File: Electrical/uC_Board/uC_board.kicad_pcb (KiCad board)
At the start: 2 copper layers, 45 x 18 mm, 27 parts, among them J1 card_edge_6p, J2 ArdStripNano, Q1 BC850, SW1 SW_Push, U1 ATmega328PB-AU, U2 AD8620, U3 LM1117MPX-5.0, X1 CSTNE16M0V530000R0

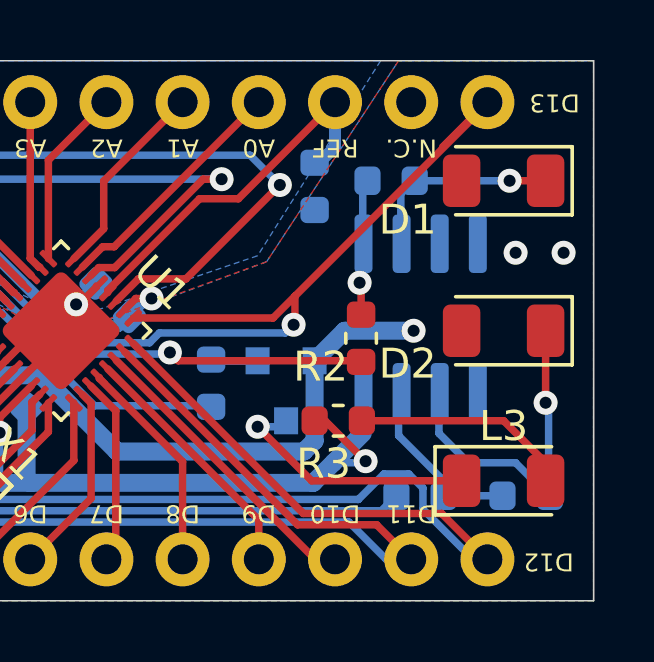
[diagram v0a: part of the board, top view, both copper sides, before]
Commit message: Updated transimpedance amp and rearranged USB board.
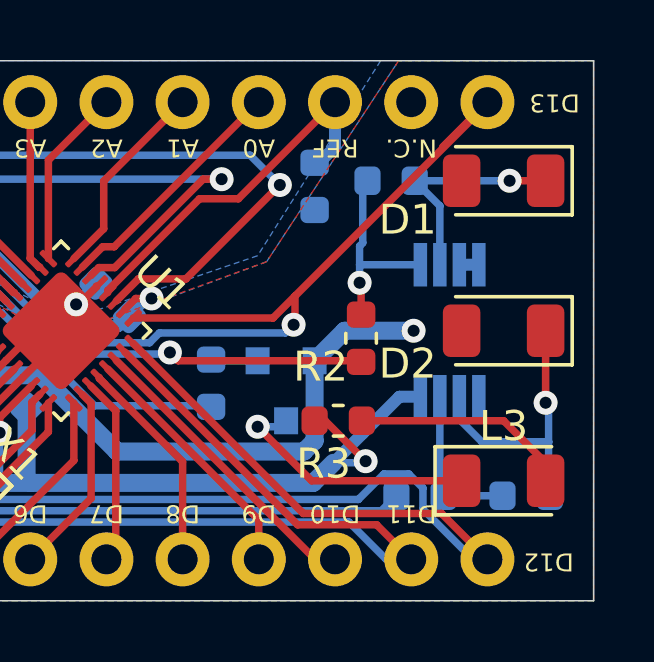
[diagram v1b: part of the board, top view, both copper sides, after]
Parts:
- J1: value card_edge_6p -> Card Edge Connector
- J2: value ArdStripNano -> Arduino Breakout Pins
- U2: value AD8620 -> OPA2381; footprint Package_SO:SOIC-8_3.9x4.9mm_P1.27mm -> Package_SO:MSOP-8_3x3mm_P0.65mm
- moved U2 1.05 mm to (140.2, 100.0)
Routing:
- net /RX: track 4.64 -> 6.67 mm
- net Net-(D2-Pad1): track 11.4 -> 9.58 mm
- net +5V: track 100.3 -> 101.3 mm
- net Net-(D1-Pad1): track 6.65 -> 7.55 mm
- net GND: track 85.2 -> 85.8 mm, vias 14 -> 12
- net Net-(C2-Pad1): track 6.25 -> 5.67 mm
